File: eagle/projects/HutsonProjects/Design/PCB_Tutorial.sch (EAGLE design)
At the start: 15 parts, among them J1 POWER_JACKPTH_BREAD, J3 AVR_SPI_PROG_3X2PTH, J4 6_PIN_SERIAL_CABLEPTH, U1 328P

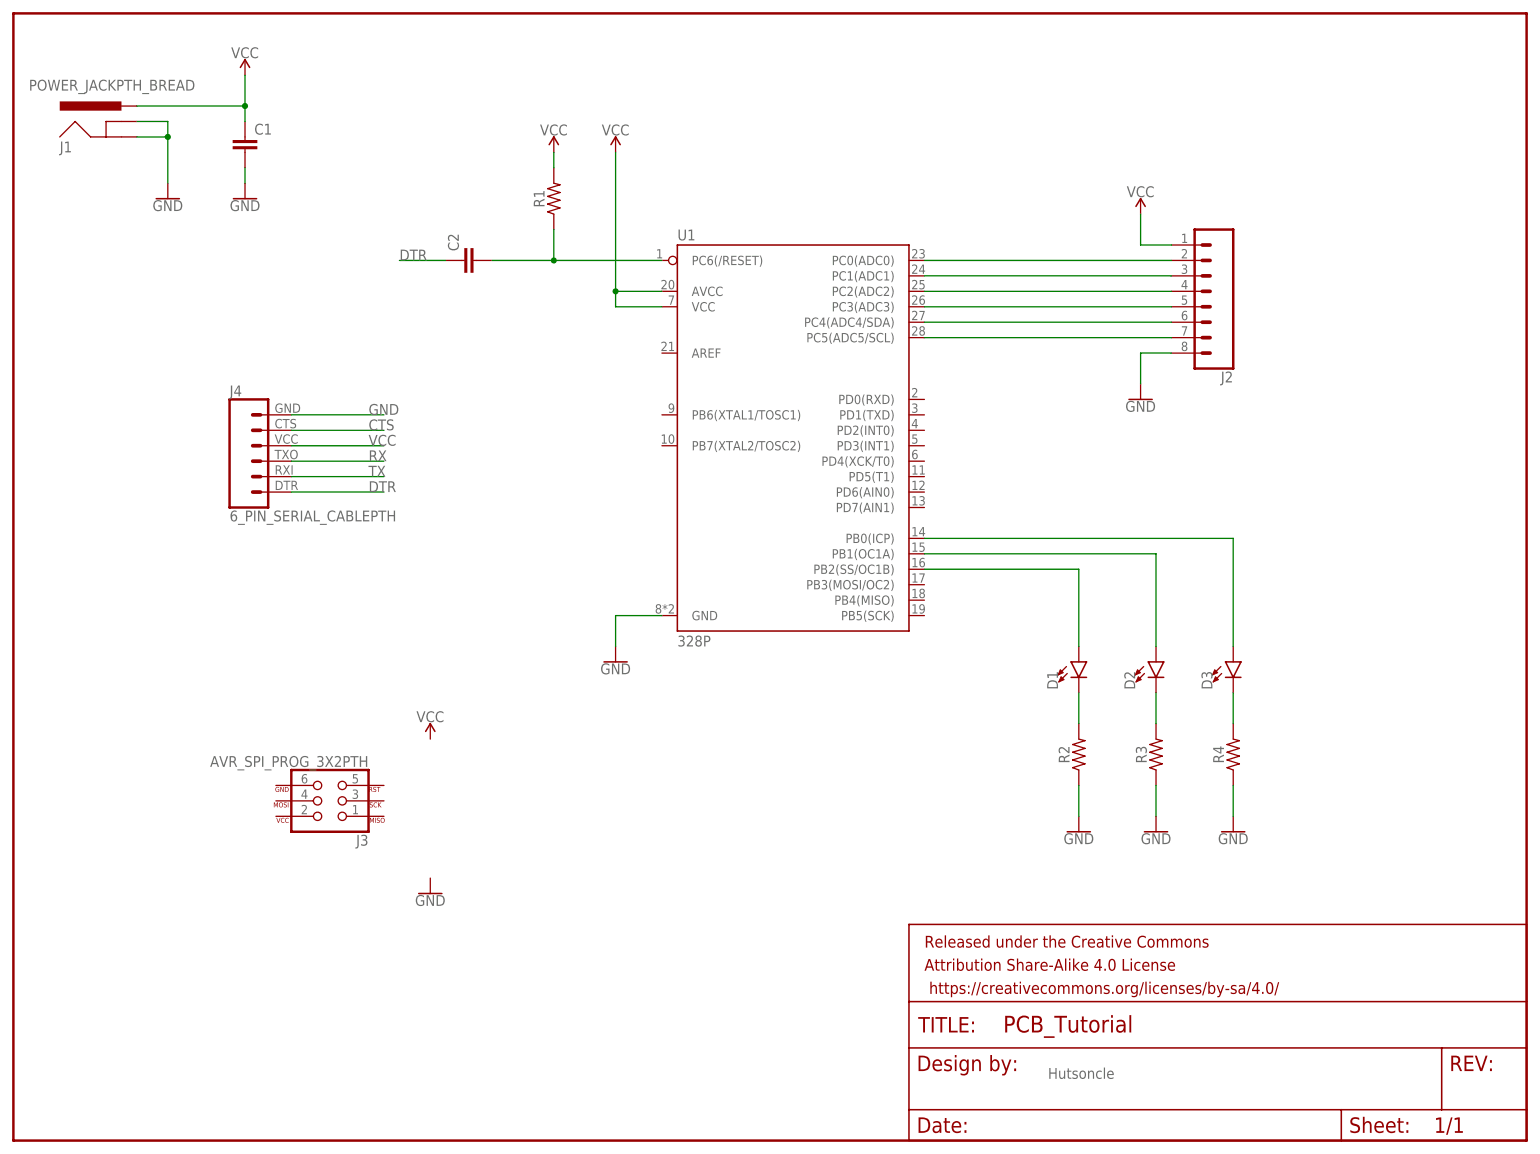
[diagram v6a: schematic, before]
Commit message: Wiring tutorial finished
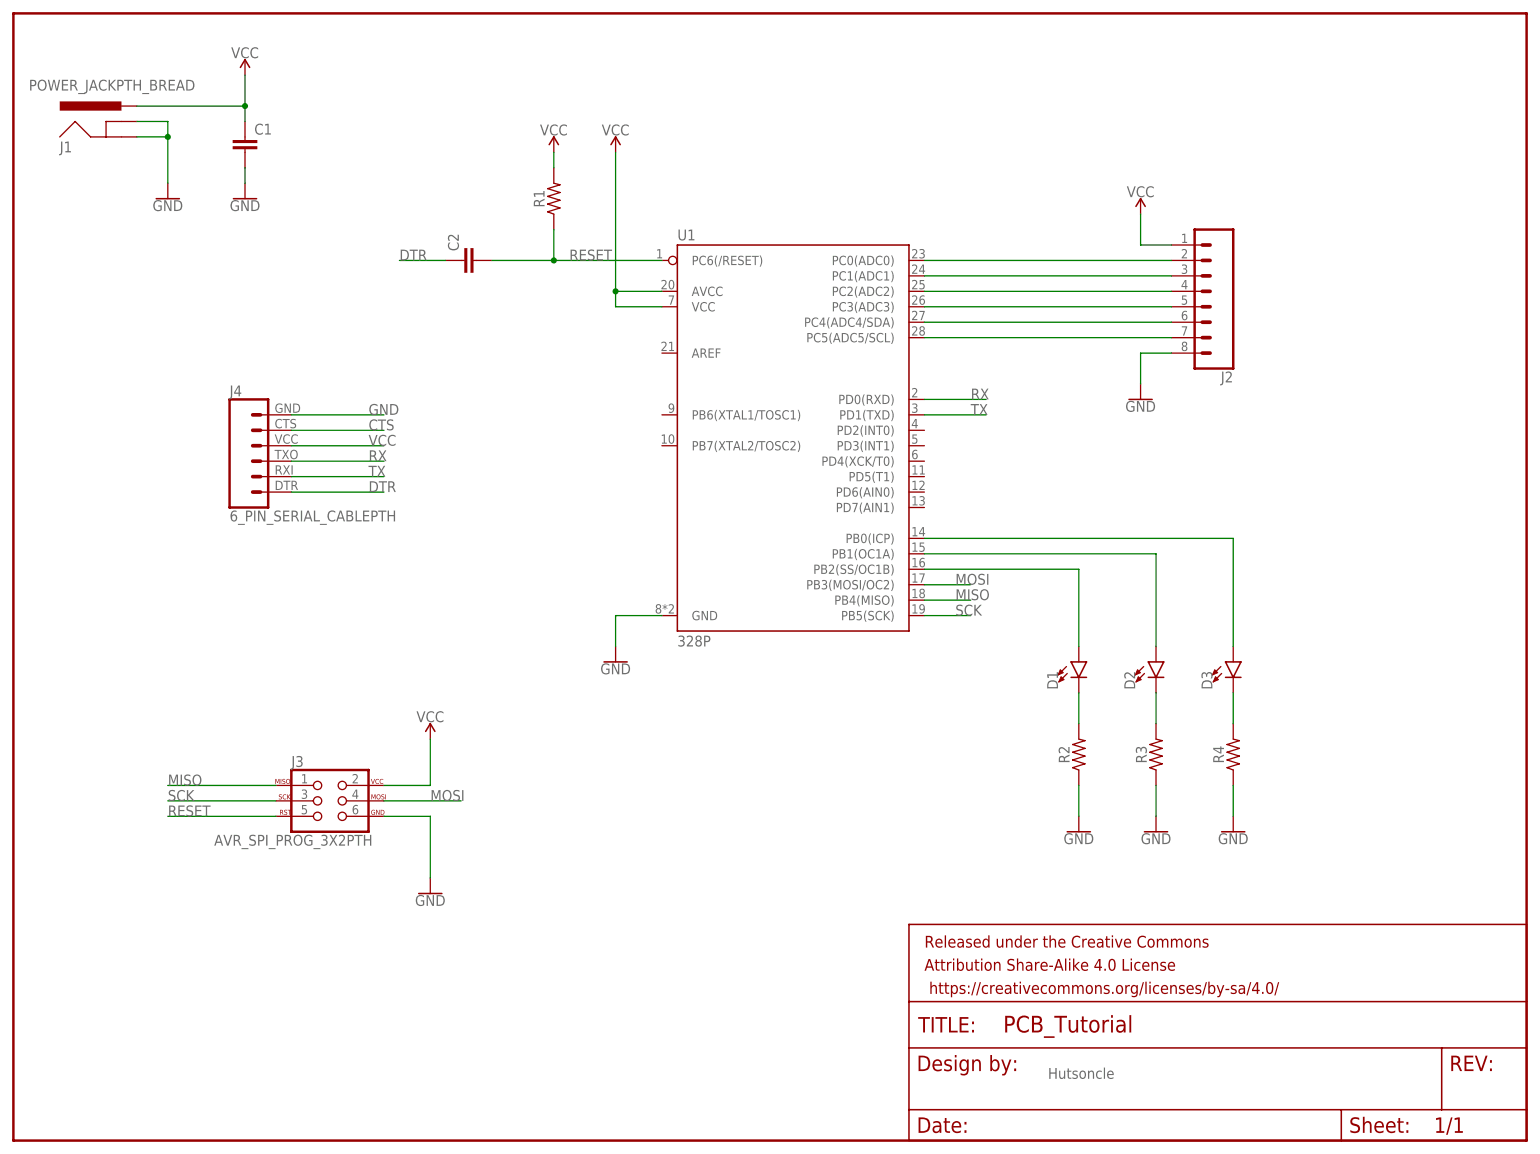
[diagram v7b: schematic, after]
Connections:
- removed net N$1: C2.2, R1.1, U1.PC6(/RESET)
- new net MISO: J3.1, U1.PB4(MISO)
- new net MOSI: J3.4, U1.PB3(MOSI/OC2)
- new net RESET: C2.2, J3.5, R1.1, U1.PC6(/RESET)
- new net SCK: J3.3, U1.PB5(SCK)
- net GND: now also J3.6
- net RX: now also U1.PD0(RXD)
- net TX: now also U1.PD1(TXD)
- net VCC: now also J3.2
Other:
- moved on the sheet: J3
